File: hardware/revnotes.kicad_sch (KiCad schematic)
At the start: 0 parts

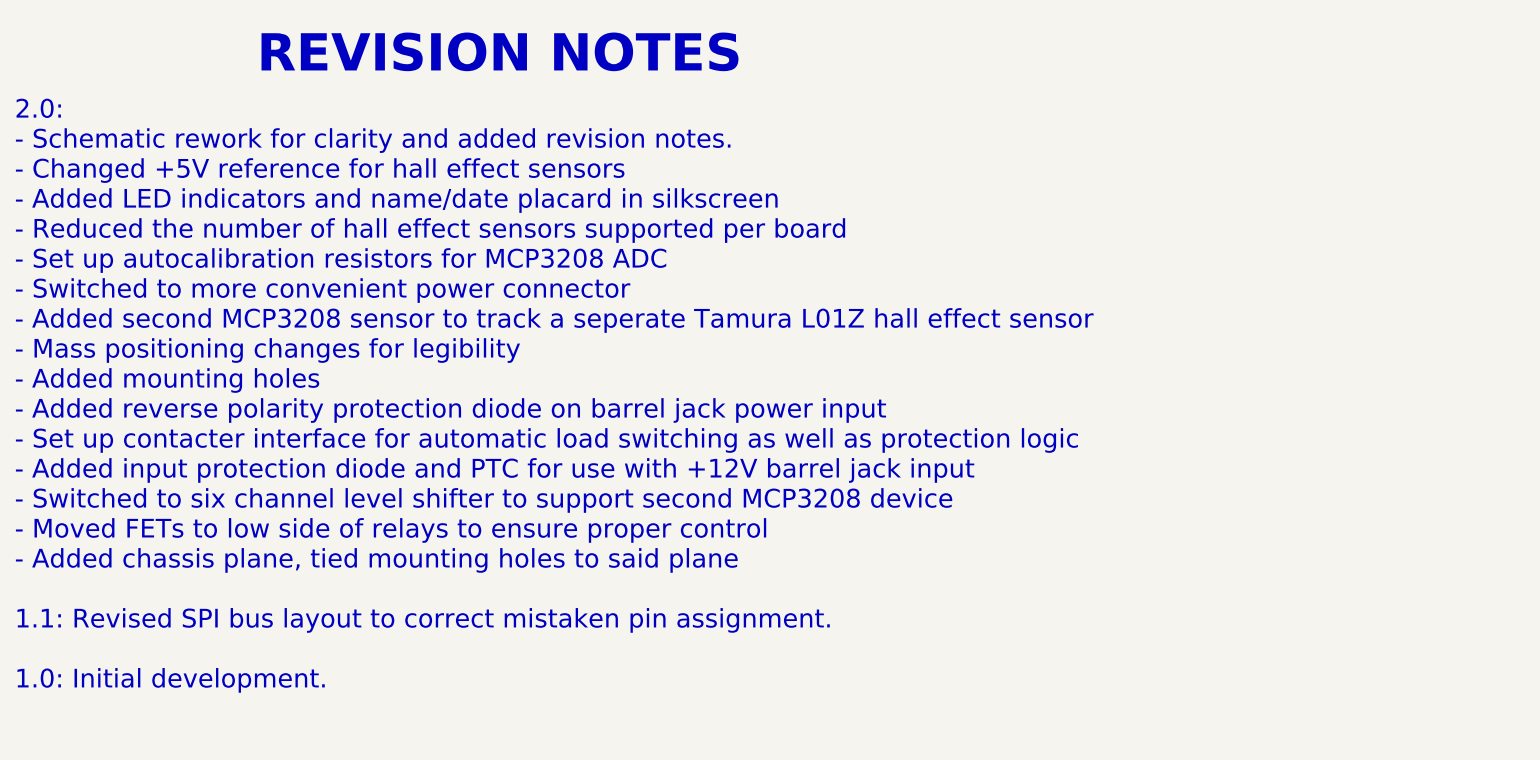
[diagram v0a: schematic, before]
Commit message: Changed jumpers to resistors for L01Z sensor, updated fab/asy docs.
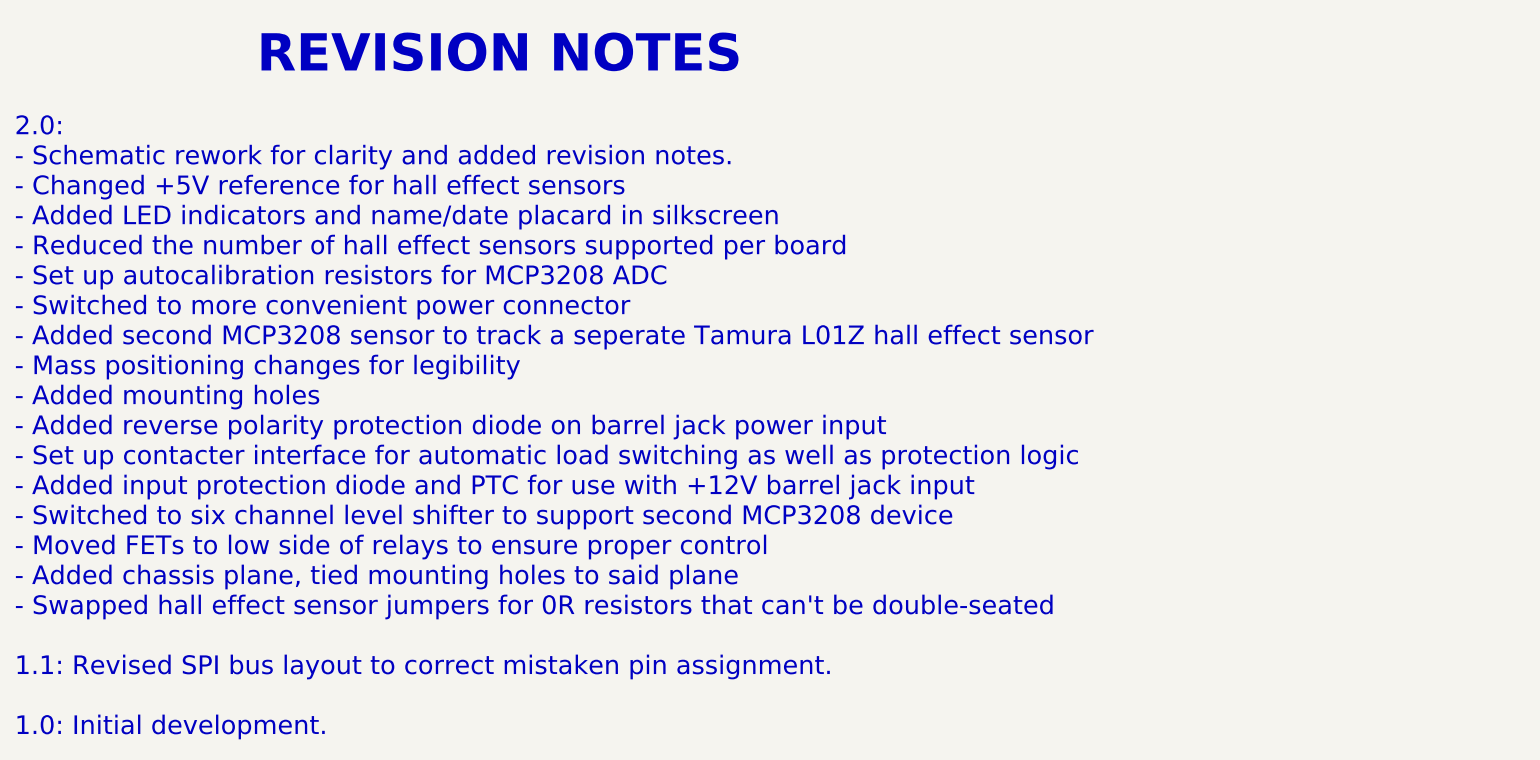
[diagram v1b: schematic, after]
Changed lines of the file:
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@@
     (comment 2 "(PENDING REVIEW)")
   )
-  (text "2.0: \n- Schematic rework for clarity and added revision notes.\n- Changed +5V reference for hall effect sensors\n- Added LED indicators and name/date placard in silkscreen\n- Reduced the number of hall effect sensors supported per board\n- Set up autocalibration resistors for MCP3208 ADC\n- Switched to more convenient power connector\n- Added second MCP3208 sensor to track a seperate Tamura L01Z hall effect sensor\n- Mass positioning changes for legibility\n- Added mounting holes\n- Added reverse polarity protection diode on barrel jack power input\n- Set up contacter interface for automatic load switching as well as protection logic\n- Added input protection diode and PTC for use with +12V barrel jack input\n- Switched to six channel level shifter to support second MCP3208 device\n- Moved FETs to low side of relays to ensure proper control\n- Added chassis plane, tied mounting holes to said plane\n\n1.1: Revised SPI bus layout to correct mistaken pin assignment.\n\n1.0: Initial development."
-    (at 83.82 121.92 0)
+  (text "2.0: \n- Schematic rework for clarity and added revision notes.\n- Changed +5V reference for hall effect sensors\n- Added LED indicators and name/date placard in silkscreen\n- Reduced the number of hall effect sensors supported per board\n- Set up autocalibration resistors for MCP3208 ADC\n- Switched to more convenient power connector\n- Added second MCP3208 sensor to track a seperate Tamura L01Z hall effect sensor\n- Mass positioning changes for legibility\n- Added mounting holes\n- Added reverse polarity protection diode on barrel jack power input\n- Set up contacter interface for automatic load switching as well as protection logic\n- Added input protection diode and PTC for use with +12V barrel jack input\n- Switched to six channel level shifter to support second MCP3208 device\n- Moved FETs to low side of relays to ensure proper control\n- Added chassis plane, tied mounting holes to said plane\n- Swapped hall effect sensor jumpers for 0R resistors that can't be double-seated\n\n1.1: Revised SPI bus layout to correct mistaken pin assignment.\n\n1.0: Initial development."
+    (at 83.82 128.27 0)
     (effects (font (size 2.54 2.54)) (justify left bottom))
   )
